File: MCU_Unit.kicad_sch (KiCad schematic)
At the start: 30 parts, among them J401 Solder Holes 4x1 2.54mm 22AWG, J402 Conn_ARM_SWD_TagConnect_TC203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, J403 Solder Wire Pad 1,5x3mm, J404 Solder Wire Pad 1,5x3mm, SW401 KMR232NG ULC, SW402 KMR232NG ULC, SW403 CAS-D20A1, SW404 KMR232NG ULC, SW405 KMR232NG ULC, SW406 KMR232NG ULC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

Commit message: Advanced rough layout
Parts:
- added C408, C409, C410: 3p3 C0G 50V, Capacitor_SMD:C_0402_1005Metric, symbol Device:C_Small
- added J407, J408: Solder Wire Pad 1,5x3mm, 0_Plume:SolderWirePad_SMD_1,5x3mm, symbol Connector_Generic:Conn_01x01
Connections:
- net 5V_ENABLE: now also U401.8 (PC2)
- net BAT_SENSE: now also U401.2 (PA1)
- net BAT_SENSE_EN: now also U401.3 (PA0)
- net BUTTON1: now also U401.18 (PB7)
- net BUTTON2: now also U401.19 (PB5)
- net BUTTON3: now also U401.20 (PB4)
- net BUTTON4: now also U401.22 (PC10)
- net DIN_3V3: now also U401.7 (PC3)
- net EN1: now also U401.56 (PA3); no longer U401.77 (PD10)
- net EN2: now also U401.1 (PA2); no longer U401.82 (PD11)
- net GND: now also C408.2, C409.2, C410.2
- net I2C3_SCL: now also J408.1 (Pin_1)
- net I2C3_SDA: now also J407.1 (Pin_1)
- net USART1_RX: now also R404.1, U401.28 (PA10); no longer D401.1 (I/O1), J401.3 (Pin_3), R404.2
- net USART1_TX: now also R403.1, U401.51 (PA9); no longer D401.3 (I/O2), J401.2 (Pin_2), R403.2
- net nFAULT3: now also C408.1
- net nFAULT4: now also C409.1
- net nFAULT5: now also C410.1
- net BOOT0_B: now reaches R401.1, SW401.1, SW401.4
- new net USART1_RX_C: D401.1 (I/O1), D401.3 (I/O2), J401.2 (Pin_2), J401.3 (Pin_3), R403.2, R404.2
- no-connect marks 42 -> 34
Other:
- moved on the sheet: D401, J401, J403, J404, R403, R404, TP401, TP402, TP403, TP404, TP405, TP406

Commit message: Finished layout, only cleaning left
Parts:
- C404: renamed from C408; now not fitted; now left out of the parts list
- C405: renamed from C409; now not fitted; now left out of the parts list
- C406: renamed from C410; now not fitted; now left out of the parts list
- J403: footprint 0_Plume:SolderWirePad_SMD_1,5x3mm -> 0_Plume:Connector_SolderWirePad_SMD_1,5x3mm
- J404: renamed from J408; footprint 0_Plume:SolderWirePad_SMD_1,5x3mm -> 0_Plume:Connector_SolderWirePad_SMD_1,5x3mm
- J405: renamed from J407; footprint 0_Plume:SolderWirePad_SMD_1,5x3mm -> 0_Plume:Connector_SolderWirePad_SMD_1,5x3mm
- J406: renamed from J404; footprint 0_Plume:SolderWirePad_SMD_1,5x3mm -> 0_Plume:Connector_SolderWirePad_SMD_1,5x3mm
- SW401, SW402, SW404, SW405, SW406, SW407: footprint 0_Plume:KMR232NGULCLFS -> 0_Plume:SW_KMR232NGULCLFS
- renumbered C404 to C407, C405 to C408, C406 to C409, C407 to C410, R609 to R402
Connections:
- net CHARGE_STATUS: now also U401.76 (PD15)
- net IMU_INT1: now also U401.67 (PD7)
- net IMU_INT2: now also U401.66 (PD12)
- net MUX_RESET: now also U401.27 (PA15)
- net SWITCH1: now also U401.72 (PE3)
- net SWITCH2: now also U401.73 (PD4)
- net USART1_RX_C: no longer D401.3 (I/O2), J401.2 (Pin_2), R403.2
- net nFAULT0: now also U401.53 (PA6); no longer U401.50 (PA8)
- net nFAULT1: now also U401.62 (PH1); no longer U401.49 (PC4)
- net nFAULT10: now also U401.54 (PA5); no longer U401.40 (PC13)
- net nFAULT11: now also U401.50 (PA8); no longer U401.39 (PB6)
- net nFAULT12: now also U401.49 (PC4); no longer U401.38 (PB15)
- net nFAULT13: now also U401.33 (PD0); no longer U401.37 (PB14)
- net nFAULT14: now also U401.70 (PD3); no longer U401.36 (PC6)
- net nFAULT16: now also U401.52 (PA7); no longer U401.34 (PD1)
- net nFAULT17: now also U401.34 (PD1); no longer U401.33 (PD0)
- net nFAULT2: now also U401.61 (PH0); no longer U401.48 (PB2)
- net nFAULT3: now also U401.63 (PD14); no longer U401.47 (PB10)
- net nFAULT4: now also U401.65 (PD13); no longer U401.46 (PB11)
- net nFAULT5: now also U401.55 (PA4); no longer U401.45 (PC5)
- net nFAULT6: now also U401.79 (PE0); no longer U401.44 (PB0)
- net nFAULT7: now also U401.78 (PE2); no longer U401.43 (PB1)
- net nFAULT8: now also U401.41 (PB12); no longer U401.42 (PE4)
- net nFAULT9: now also U401.42 (PE4); no longer U401.41 (PB12)
- net nSLEEP_FRONT: now also U401.64 (PE1)
- net nSLEEP_REAR: now also U401.71 (PC7)
- net ~{RESET}: no longer SW402.2
- new net USART1_TX_C: D401.3 (I/O2), J401.2 (Pin_2), R403.2
- no-connect marks 34 -> 26

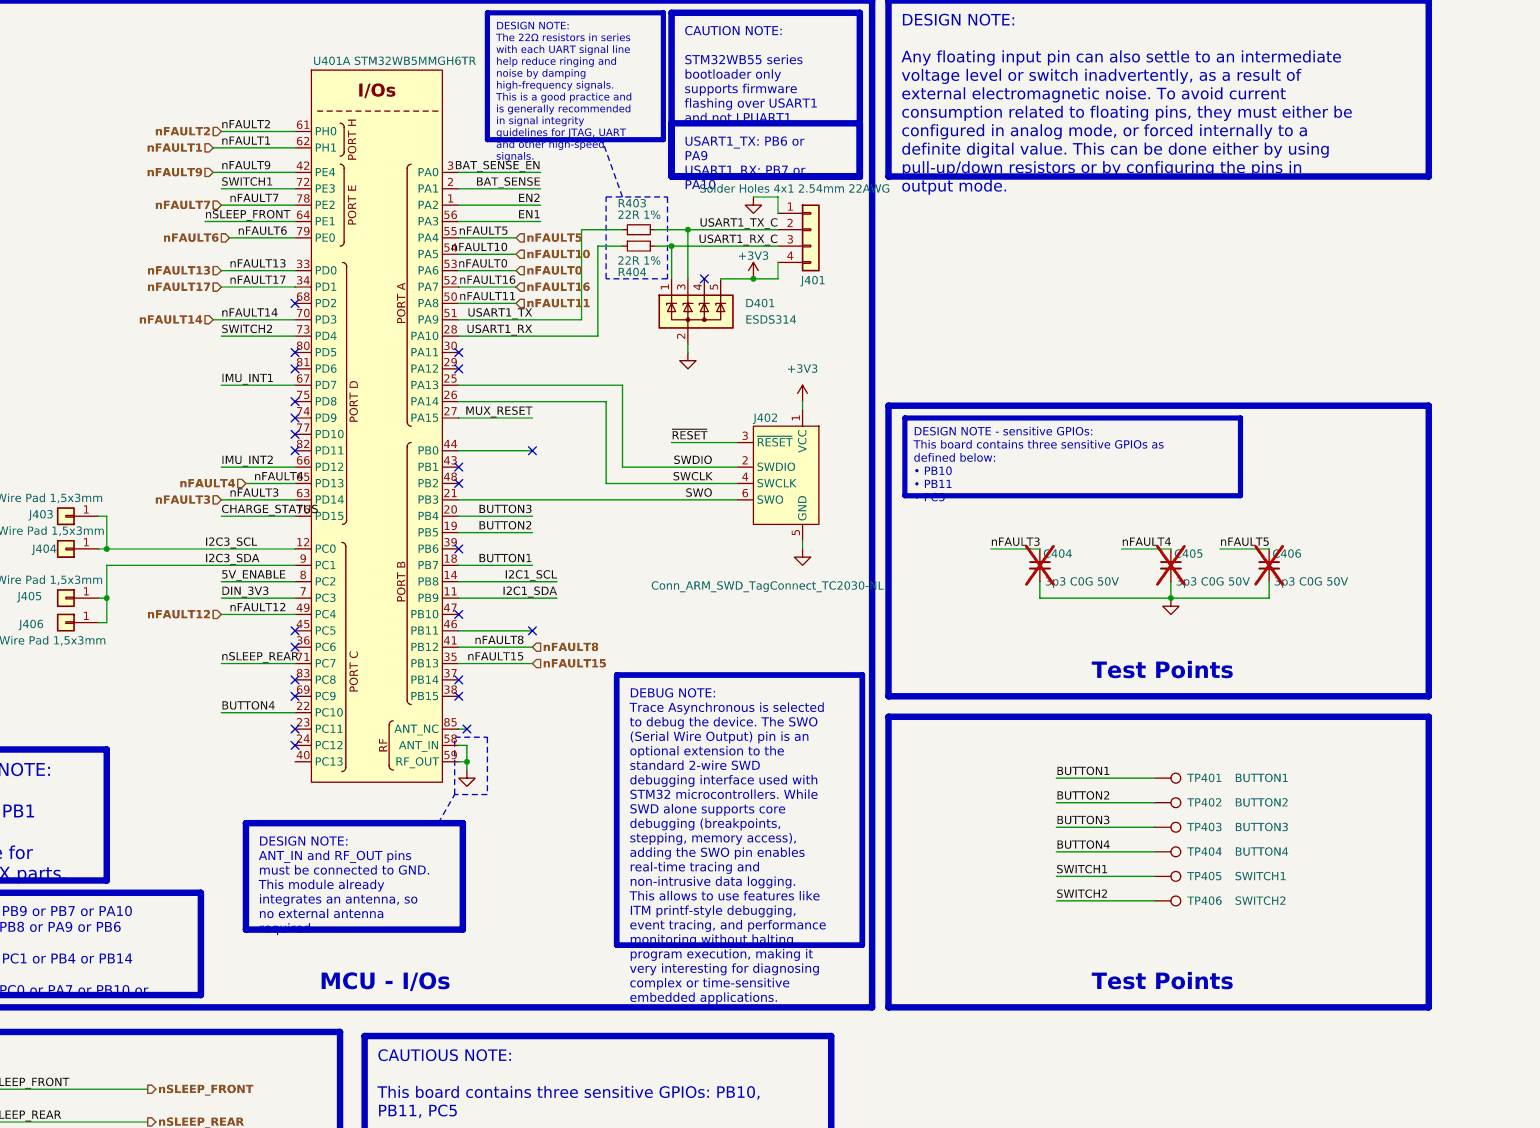
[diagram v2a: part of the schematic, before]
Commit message: Finished cleaning routing, removed errors, cleaned shematics, added pictures and other improvements
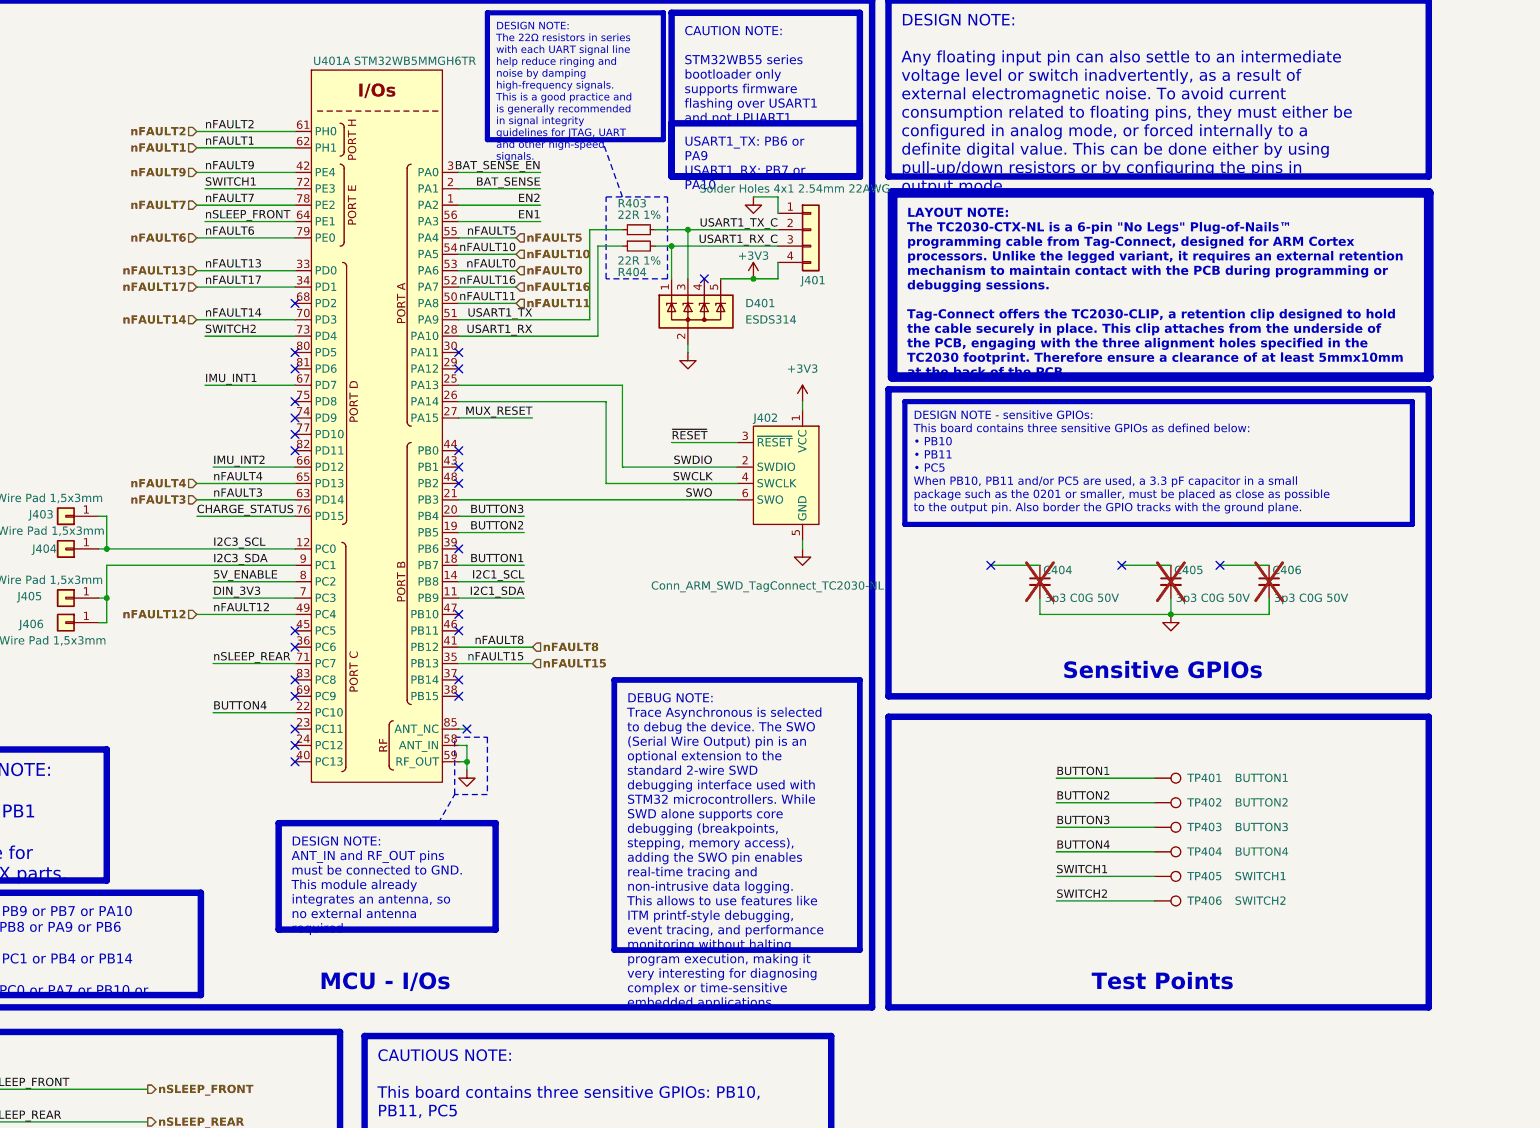
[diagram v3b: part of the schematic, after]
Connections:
- net nFAULT3: no longer C404.1
- net nFAULT4: no longer C405.1
- net nFAULT5: no longer C406.1
- no-connect marks 26 -> 30
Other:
- moved on the sheet: C404, C405, C406
